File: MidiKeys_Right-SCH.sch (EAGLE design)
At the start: 73 parts, among them J1 3M 8550-4500

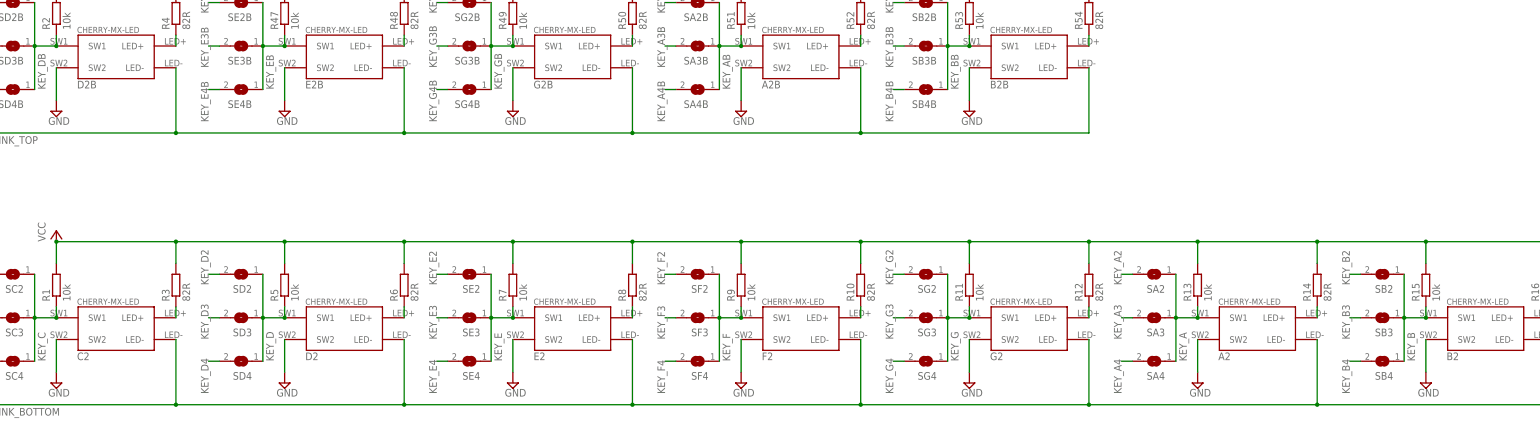
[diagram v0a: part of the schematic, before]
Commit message: placed solder bridges in correct places
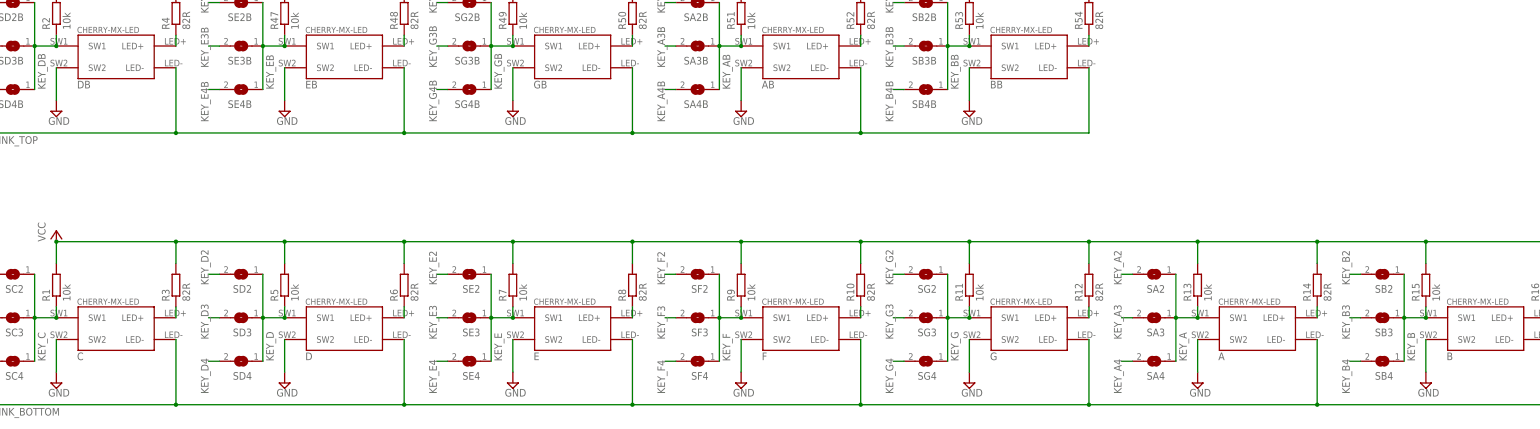
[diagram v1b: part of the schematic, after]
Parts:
- renumbered A2 to A, A2B to AB, B2 to B, B2B to BB, C2 to C, D2 to D, D2B to DB, E2 to E, E2B to EB, F2 to F, G2 to G, G2B to GB
